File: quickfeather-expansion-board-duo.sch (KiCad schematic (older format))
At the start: 5 parts, among them J1 QuickFeather, J2 1x4_Conn, J3 1x4_Conn, J4 QuickFeather, J5 UDA1334

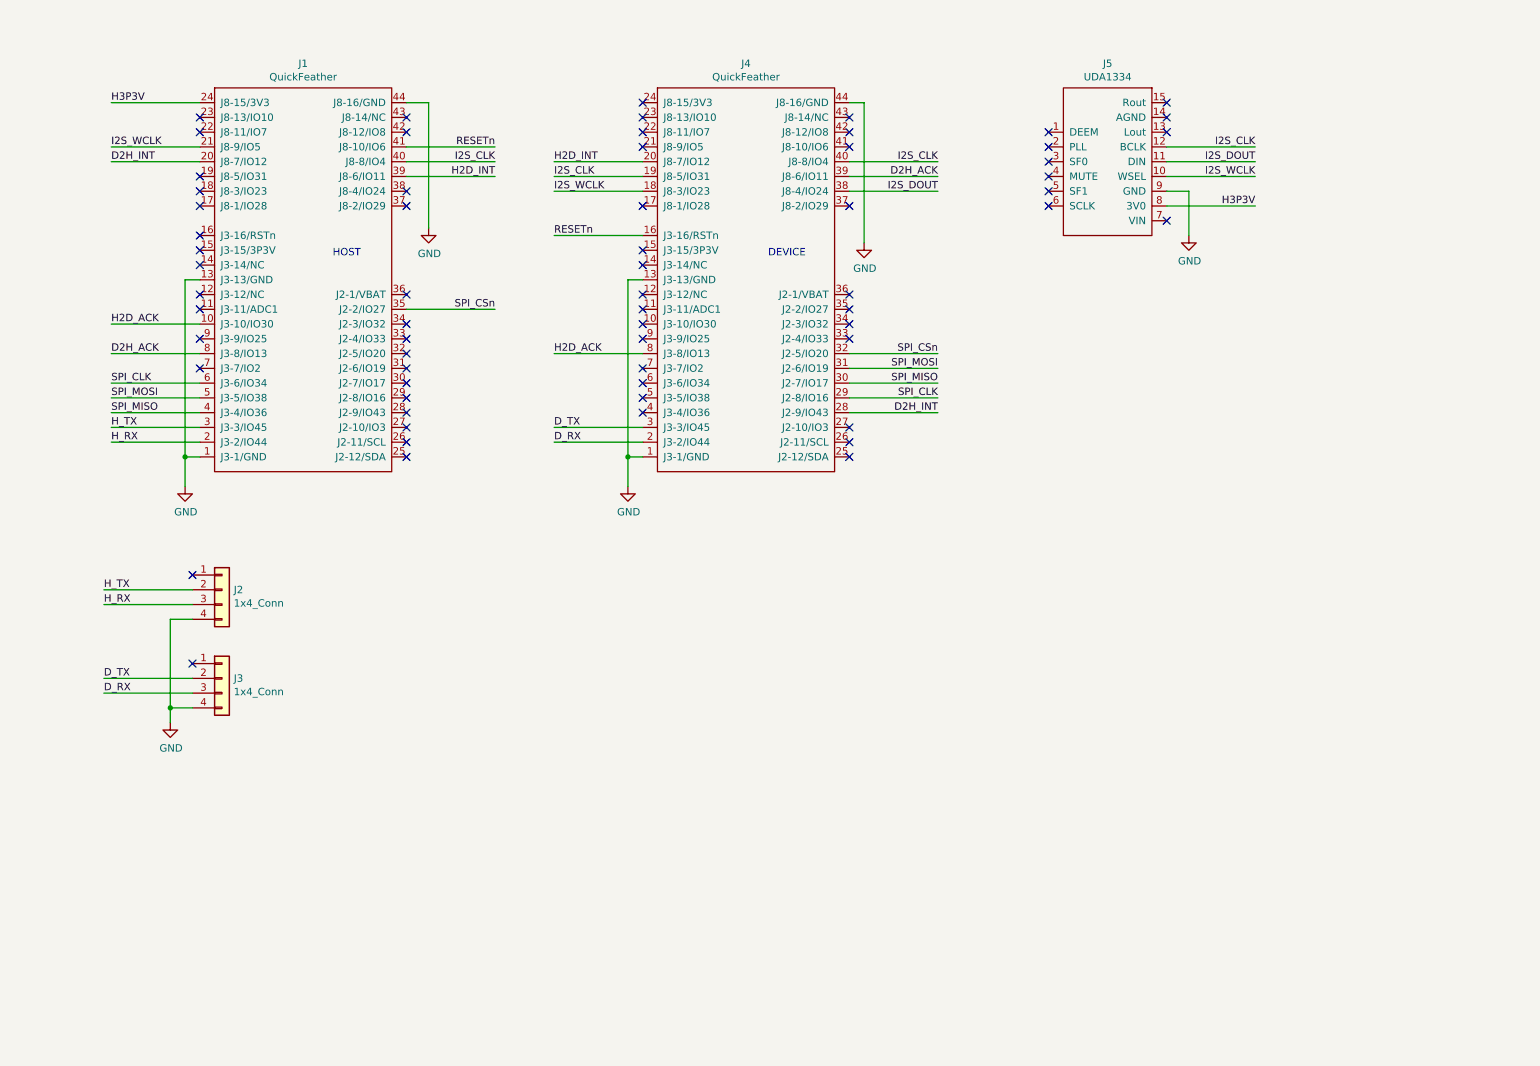
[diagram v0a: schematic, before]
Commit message: 1st Rev of schematic Part Placement - partial
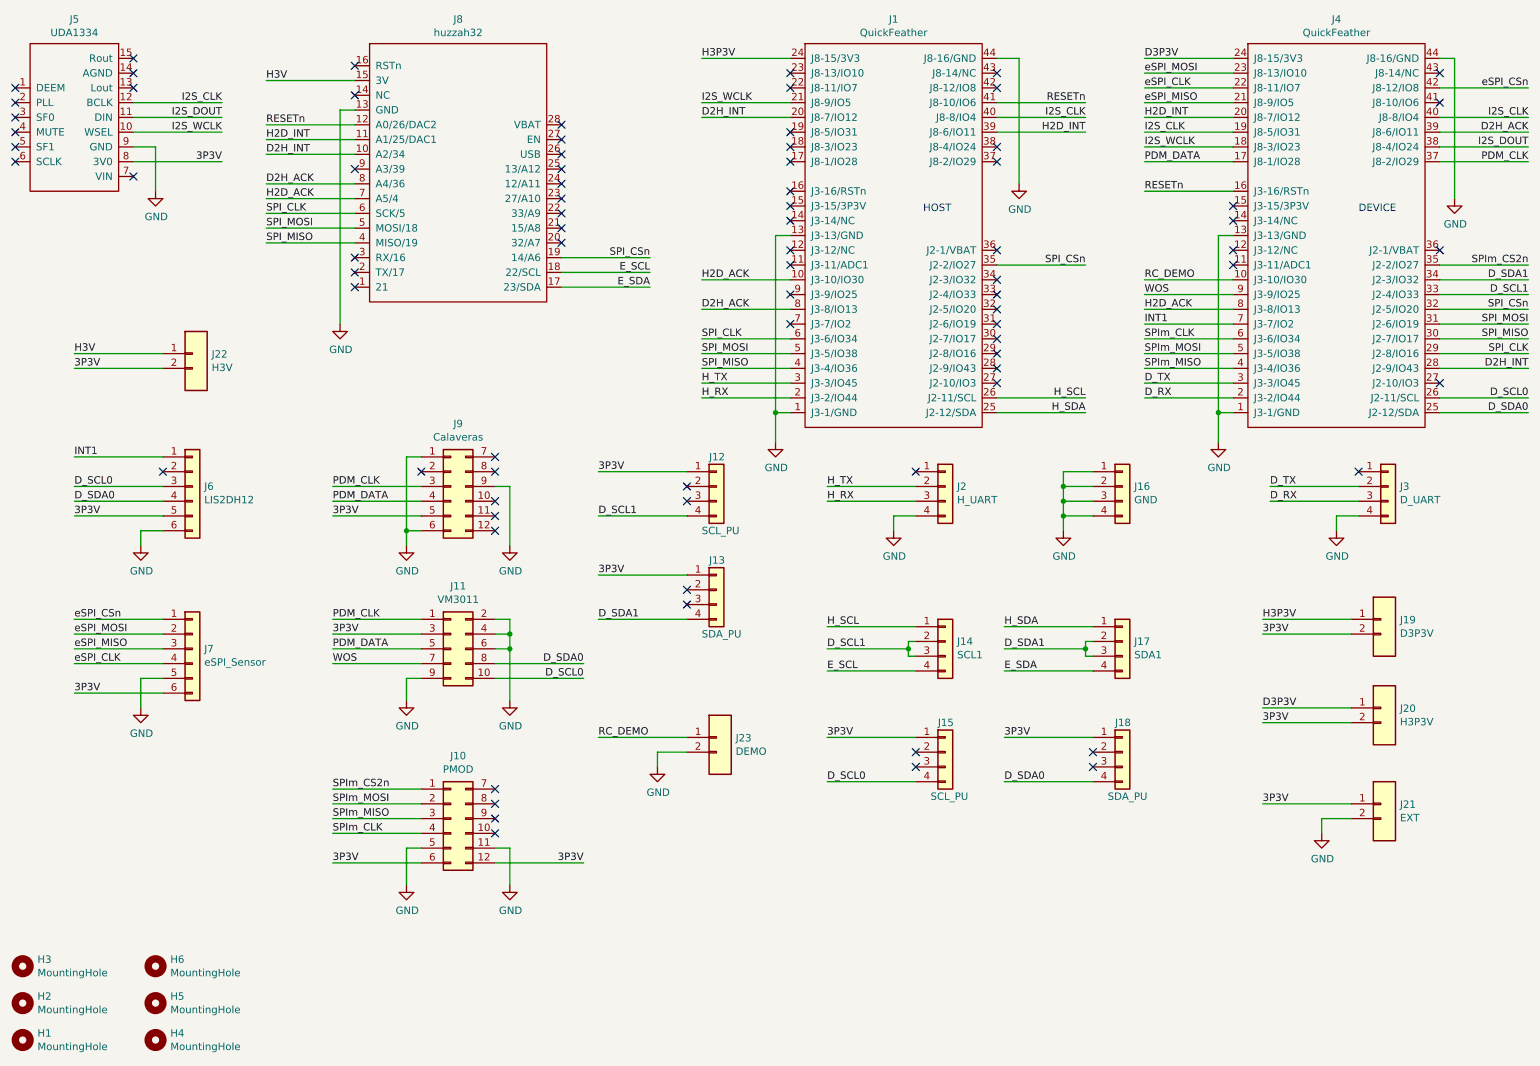
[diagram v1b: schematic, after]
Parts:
- added H1, H2, H3, H4, H5, H6: MountingHole, MPAD, symbol Mechanical:MountingHole
- added J10: PMOD, quicklogicBoards-footprints:2x6_Conn, symbol quicklogicBoardsSympbols:2x6_Conn
- added J11: VM3011, quicklogicBoards-footprints:2x5_Conn, symbol quicklogicBoardsSympbols:2x5_Conn
- added J12, J15: SCL_PU, quicklogicBoards-footprints:1x4_Conn, symbol quicklogicBoardsSympbols:1x4_Conn
- added J13, J18: SDA_PU, quicklogicBoards-footprints:1x4_Conn, symbol quicklogicBoardsSympbols:1x4_Conn
- added J14: SCL1, quicklogicBoards-footprints:1x4_Conn, symbol quicklogicBoardsSympbols:1x4_Conn
- added J16: GND, quicklogicBoards-footprints:1x4_Conn, symbol quicklogicBoardsSympbols:1x4_Conn
- added J17: SDA1, quicklogicBoards-footprints:1x4_Conn, symbol quicklogicBoardsSympbols:1x4_Conn
- added J19: D3P3V, quicklogicBoards-footprints:1x2_Conn, symbol quicklogicBoardsSympbols:1x2_Conn
- added J20: H3P3V, quicklogicBoards-footprints:1x2_Conn, symbol quicklogicBoardsSympbols:1x2_Conn
- added J21: EXT, quicklogicBoards-footprints:1x2_Conn, symbol quicklogicBoardsSympbols:1x2_Conn
- added J22: H3V, quicklogicBoards-footprints:1x2_Conn, symbol quicklogicBoardsSympbols:1x2_Conn
- added J23: DEMO, quicklogicBoards-footprints:1x2_Conn, symbol quicklogicBoardsSympbols:1x2_Conn
- added J6: LIS2DH12, quicklogicBoards-footprints:1x6_Conn, symbol quicklogicBoardsSympbols:1x6_Conn
- added J7: eSPI_Sensor, quicklogicBoards-footprints:1x6_pinhead, symbol quicklogicBoardsSympbols:1x6_Conn
- added J8: huzzah32, quicklogicBoards-footprints:huzzah32, symbol quicklogicBoardsSympbols:huzzah32
- added J9: Calaveras, quicklogicBoards-footprints:2x6_Conn, symbol quicklogicBoardsSympbols:2x6_Conn
- J2: value 1x4_Conn -> H_UART
- J3: value 1x4_Conn -> D_UART
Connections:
- net D2H_ACK: now also J8.8 (A4/36)
- net D2H_INT: now also J8.10 (A2/34)
- net GND: now also J10.11, J10.5, J11.2, J11.4, J11.6, J11.9, J16.1, J16.2, J16.3, J16.4, J21.2, J23.2, J6.6, J7.5, J8.13 (GND), J9.1, J9.6, J9.9
- net H2D_ACK: now also J8.7 (A5/4)
- net H2D_INT: now also J8.11 (A1/25/DAC1)
- net H3P3V: now also J19.1; no longer J5.8 (3V0)
- net RESETn: now also J8.12 (A0/26/DAC2)
- net SPI_CLK: now also J8.6 (SCK/5)
- net SPI_CSn: now also J8.19 (14/A6)
- net SPI_MISO: now also J8.4 (MISO/19)
- net SPI_MOSI: now also J8.5 (MOSI/18)
- net H_SDA: now reaches J1.25 (J2-12/SDA)
- net H_SDA: now also J17.1
- net H_SCL: now reaches J1.26 (J2-11/SCL)
- net H_SCL: now also J14.1
- net RC_DEMO: now reaches J4.10 (J3-10/IO30)
- net RC_DEMO: now also J23.1
- net PDM_DATA: now reaches J4.17 (J8-1/IO28)
- net PDM_DATA: now also J11.5, J9.4
- net eSPI_MISO: now reaches J4.21 (J8-9/IO5)
- net eSPI_MISO: now also J7.3
- net eSPI_CLK: now reaches J4.22 (J8-11/IO7)
- net eSPI_CLK: now also J7.4
- net eSPI_MOSI: now reaches J4.23 (J8-13/IO10)
- net eSPI_MOSI: now also J7.2
- net D3P3V: now reaches J4.24 (J8-15/3V3)
- net D3P3V: now also J20.1
- net D_SDA0: now reaches J4.25 (J2-12/SDA)
- net D_SDA0: now also J11.8, J18.4, J6.4
- net D_SCL0: now reaches J4.26 (J2-11/SCL)
- net D_SCL0: now also J11.10, J15.4, J6.3
- net D_SCL1: now reaches J4.33 (J2-4/IO33)
- net D_SCL1: now also J12.4, J14.2, J14.3
- net D_SDA1: now reaches J4.34 (J2-3/IO32)
- net D_SDA1: now also J13.4, J17.2, J17.3
- net SPIm_CS2n: now reaches J4.35 (J2-2/IO27)
- net SPIm_CS2n: now also J10.1
- net PDM_CLK: now reaches J4.37 (J8-2/IO29)
- net PDM_CLK: now also J11.1, J9.3
- net SPIm_MISO: now reaches J4.4 (J3-4/IO36)
- net SPIm_MISO: now also J10.3
- net eSPI_CSn: now reaches J4.42 (J8-12/IO8)
- net eSPI_CSn: now also J7.1
- net SPIm_MOSI: now reaches J4.5 (J3-5/IO38)
- net SPIm_MOSI: now also J10.2
- net SPIm_CLK: now reaches J4.6 (J3-6/IO34)
- net SPIm_CLK: now also J10.4
- net INT1: now reaches J4.7 (J3-7/IO2)
- net INT1: now also J6.1
- net WOS: now reaches J4.9 (J3-9/IO25)
- net WOS: now also J11.7
- new net 3P3V: J10.12, J10.6, J11.3, J12.1, J13.1, J15.1, J18.1, J19.2, J20.2, J21.1, J22.2, J5.8 (3V0), J6.5, J7.6, J9.5
- new net E_SCL: J14.4, J8.18 (22/SCL)
- new net E_SDA: J17.4, J8.17 (23/SDA)
- new net H3V: J22.1, J8.15 (3V)
- no-connect marks 65 -> 79
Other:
- moved on the sheet: J1, J2, J3, J4, J5

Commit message: Submit: 1. Latest layout 2. generated schematic 3. Gerber files 4. Updated layout library
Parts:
- removed H5, H6: MountingHole, MPAD, symbol Mechanical:MountingHole
- added N1: ql_logo, quicklogicBoards-footprints:Ql_logo, symbol quicklogicBoardsSympbols:ql_logo
- J1: value QuickFeather -> QF HOST
- J12: value SCL_PU -> SCL1_PU
- J13: value SDA_PU -> SDA1_PU
- J15: value SCL_PU -> SCL0_PU
- J18: value SDA_PU -> SDA0_PU
- J19: value D3P3V -> H3P3V
- J20: value H3P3V -> D3P3V
- J4: value QuickFeather -> QF DEVICE
- J8: value huzzah32 -> HUZZAH32-QWIIC
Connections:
- net D3P3V: now also J4.15 (J3-15/3P3V); no longer J4.24 (J8-15/3V3)
- net H3P3V: now also J1.15 (J3-15/3P3V); no longer J1.24 (J8-15/3V3)
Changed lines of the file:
@@
 P 6100 3400
 F 0 "J1" H 6700 6165 50  0000 C CNN
-F 1 "QuickFeather" H 6700 6074 50  0000 C CNN
+F 1 "QF HOST" H 6700 6074 50  0000 C CNN
 F 2 "quicklogicBoards-footprints:quickfeather" H 6700 6100 50  0001 C CNN
 F 3 "" H 6700 6100 50  0001 C CNN
@@
 P 9100 3400
 F 0 "J4" H 9700 6165 50  0000 C CNN
-F 1 "QuickFeather" H 9700 6074 50  0000 C CNN
+F 1 "QF DEVICE" H 9700 6074 50  0000 C CNN
 F 2 "quicklogicBoards-footprints:quickfeather" H 9700 6100 50  0001 C CNN
 F 3 "" H 9700 6100 50  0001 C CNN
@@
 Text Label 5400 2400 0    50   ~ 0
 H2D_ACK
-Wire Wire Line
-	5400 900  6000 900
-Text Label 5400 900  0    50   ~ 0
-H3P3V
 $Comp
 L power:GND #PWR02
@@
 NoConn ~ 6000 1600
 NoConn ~ 6000 1800
-NoConn ~ 6000 1900
 NoConn ~ 6000 2000
 NoConn ~ 6000 2200
@@
 Text Label 11000 1300 2    50   ~ 0
 I2S_CLK
-NoConn ~ 9000 1900
 NoConn ~ 9000 2000
 NoConn ~ 9000 2200
@@
 P 3150 2550
 F 0 "J8" H 3750 4465 50  0000 C CNN
-F 1 "huzzah32" H 3750 4374 50  0000 C CNN
+F 1 "HUZZAH32-QWIIC" H 3750 4374 50  0000 C CNN
 F 2 "quicklogicBoards-footprints:huzzah32" H 3725 4375 50  0001 C CNN
 F 3 "" H 3725 4375 50  0001 C CNN
@@
 NoConn ~ 3050 2350
 NoConn ~ 3050 2450
-Wire Wire Line
-	8400 900  9000 900
-Text Label 8400 900  0    50   ~ 0
-D3P3V
 $Comp
 L power:GND #PWR016
@@
 $EndComp
 $Comp
-L Mechanical:MountingHole H5
-U 1 1 5FAB91FD
-P 1700 7300
-F 0 "H5" H 1800 7346 50  0000 L CNN
-F 1 "MountingHole" H 1800 7255 50  0000 L CNN
-F 2 "MPAD" H 1700 7300 50  0001 C CNN
-F 3 "~" H 1700 7300 50  0001 C CNN
-	1    1700 7300
-	1    0    0    -1
-$EndComp
-$Comp
-L Mechanical:MountingHole H6
-U 1 1 5FABEFD1
-P 1700 7050
-F 0 "H6" H 1800 7096 50  0000 L CNN
-F 1 "MountingHole" H 1800 7005 50  0000 L CNN
-F 2 "MPAD" H 1700 7050 50  0001 C CNN
-F 3 "~" H 1700 7050 50  0001 C CNN
-	1    1700 7050
-	1    0    0    -1
-$EndComp
-$Comp
 L quicklogicBoardsSympbols:1x2_Conn J19
 U 1 1 5FAC99F7
 P 10000 5200
 F 0 "J19" H 10130 5696 50  0000 L CNN
-F 1 "D3P3V" H 10130 5605 50  0000 L CNN
+F 1 "H3P3V" H 10130 5605 50  0000 L CNN
 F 2 "quicklogicBoards-footprints:1x2_Conn" H 10000 5900 50  0001 C CNN
 F 3 "" H 10000 5900 50  0001 C CNN
@@
 P 10000 5800
 F 0 "J20" H 10130 6296 50  0000 L CNN
-F 1 "H3P3V" H 10130 6205 50  0000 L CNN
+F 1 "D3P3V" H 10130 6205 50  0000 L CNN
 F 2 "quicklogicBoards-footprints:1x2_Conn" H 10000 6500 50  0001 C CNN
 F 3 "" H 10000 6500 50  0001 C CNN
@@
 P 5500 4300
 F 0 "J12" H 5450 5000 50  0000 L CNN
-F 1 "SCL_PU" H 5400 4500 50  0000 L CNN
+F 1 "SCL1_PU" H 5400 4500 50  0000 L CNN
 F 2 "quicklogicBoards-footprints:1x4_Conn" H 5500 5000 50  0001 C CNN
 F 3 "" H 5500 5000 50  0001 C CNN
@@
 P 5500 5000
 F 0 "J13" H 5450 5700 50  0000 L CNN
-F 1 "SDA_PU" H 5400 5200 50  0000 L CNN
+F 1 "SDA1_PU" H 5400 5200 50  0000 L CNN
 F 2 "quicklogicBoards-footprints:1x4_Conn" H 5500 5700 50  0001 C CNN
 F 3 "" H 5500 5700 50  0001 C CNN
@@
 P 8250 6100
 F 0 "J18" H 8200 6800 50  0000 L CNN
-F 1 "SDA_PU" H 8150 6300 50  0000 L CNN
+F 1 "SDA0_PU" H 8150 6300 50  0000 L CNN
 F 2 "quicklogicBoards-footprints:1x4_Conn" H 8250 6800 50  0001 C CNN
 F 3 "" H 8250 6800 50  0001 C CNN
@@
 P 7050 6100
 F 0 "J15" H 7000 6800 50  0000 L CNN
-F 1 "SCL_PU" H 6950 6300 50  0000 L CNN
+F 1 "SCL0_PU" H 6950 6300 50  0000 L CNN
 F 2 "quicklogicBoards-footprints:1x4_Conn" H 7050 6800 50  0001 C CNN
 F 3 "" H 7050 6800 50  0001 C CNN
@@
 Text Label 1150 3900 0    50   ~ 0
 D_SDA0
+Wire Wire Line
+	5400 1900 6000 1900
+Text Label 5400 1900 0    50   ~ 0
+H3P3V
+NoConn ~ 6000 900
+Wire Wire Line
+	8400 1900 9000 1900
+Text Label 8400 1900 0    50   ~ 0
+D3P3V
+NoConn ~ 9000 900
+$Comp
+L quicklogicBoardsSympbols:ql_logo N1
+U 1 1 5FAC1E49
+P 5100 6950
+F 0 "N1" H 5294 6998 50  0000 L CNN
+F 1 "ql_logo" H 5294 6907 50  0000 L CNN
+F 2 "quicklogicBoards-footprints:Ql_logo" H 5294 6816 50  0000 L CNN
+F 3 "" H 5100 6950 50  0001 C CNN
+	1    5100 6950
+	1    0    0    -1
+$EndComp
 $EndSCHEMATC
